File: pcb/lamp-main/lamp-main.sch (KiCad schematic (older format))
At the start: 37 parts, among them IC1 ATMEGA328P, IC2 LM1117, IC3 TLC5973, J1 5V_OUT, J2 LED_CARD_BOTTOM, P1 7-12V_IN, P2 AVR_ISP, P3 SERIAL, P4 LEDSTACK, P5 LEDSTACK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

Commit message: this is going somewhere
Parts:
- removed C10, C11: 0.1uF, symbol C
- removed IC3: TLC5973, symbol TLC5973
- removed J2: LED_CARD_BOTTOM, symbol 5PIN_FEMALE
- removed LED1, LED2: CREE-CLV6A-FKB, symbol CREE-CLV6A-FKB
- removed P7: LED_CARD_TOP, symbol 5PIN_MALE
- removed P8: SER_SHORT, symbol 5PIN_MALE
- removed R4: 2kΩ, symbol R
- removed R5: 1kΩ, symbol R
- removed S1: TOP, symbol SPDT
- LED_HRT: renamed from LED3; value HEART -> RED
- LED_PWR: renamed from LED4; value PWR -> RED
- P1: value 7-12V_IN -> 5-12V_IN
- Y1: value 14.7456MHz -> 8MHz
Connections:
- net labels added: ADC_6, ADC_7, ADC_C3, ADC_C4, ADC_C5, DIO_B1, DIO_B2, DIO_D4, INT_0, INT_1
- net labels removed: BLU, GRN, LED_GND, LED_SER_IN, LED_SER_OUT, RED, SENSE_BOT, SENSE_TOP, VLED, VLOG, VLOG_TOP
- wire segments 143 -> 101
- no-connect marks 10 -> 2
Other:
- note added: "3.3V input and optional regulator"
- note removed: "7-12 V Input/Output and 5V Regulator"
- note removed: "LED Board (Multiple)"
- moved on the sheet: LED_HRT, LED_PWR, R1, R2, R3, R6, R7

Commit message: main board edits first pass done
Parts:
- removed J1: 5V_OUT, symbol 2PIN_FEMALE
- added P10: VCC, symbol 2PIN_MALE
- added P7: USER-INPUT, symbol 5PIN_MALE
- added P8: EXTRA-IO, symbol 2PIN_MALE
- added P9: WIFI, symbol 3PIN_MALE
- C7: value 10uF -> DNP(10uF)
- C8: value 22uF -> DNP(22uF)
- IC2: value LM1117 -> DNP(LM1117_3.3)
- P1: value 5-12V_IN -> VLED_IN
- Y1: Distrib. Link http://www.digikey.com/product-detail/en/ABLS-14.7456MHZ-B4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 -> http://www.digikey.com/product-detail/en/ABM2-8.000MHZ-D4Y-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; Distrib. Part 535-10223-1-ND -> 535-10870-1-ND; Manuf. Part ABLS-14.7456MHZ-B4-T -> ABM2-8.000MHZ-D4Y-T
- renumbered LED_HRT to LED1, LED_PWR to LED2
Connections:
- net labels added: BUTTON_0, BUTTON_1, POT_0, POT_1, POT_2, WIFI_EN, WIFI_IRQ, WIFI_SS
- net labels removed: ADC_6, ADC_7, ADC_C5, DIO_B1, DIO_B2, DIO_D4, INT_0, INT_1
- wire segments 101 -> 113
- no-connect marks 2 -> 0
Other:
- note added: "ATMega 328P microcontroller"
- note added: "led stacks"
- note added: "programming and communication"
- note added: "user input and extra io"
- note removed: "LED Stack Headers"
- note removed: "MCU"
- note removed: "Programming and Communication Headers"
- moved on the sheet: C9, LED1, LED2, P2, P3, R6, R7

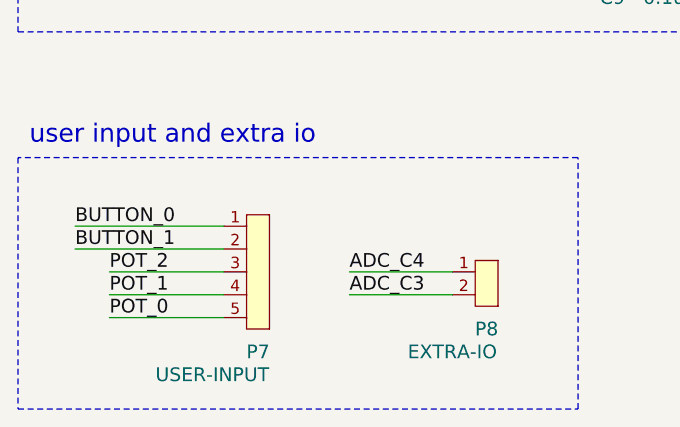
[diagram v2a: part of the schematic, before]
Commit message: still need to add boost reg to schematic;
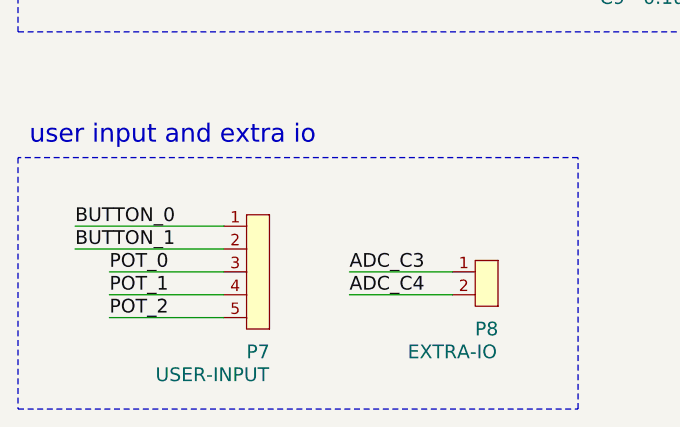
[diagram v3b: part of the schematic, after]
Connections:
- net ADC_C3: now also P8.1; no longer P8.2
- net ADC_C4: now also P8.2; no longer P8.1
- net POT_0: now also P7.3; no longer P7.5
- net POT_2: now also P7.5; no longer P7.3
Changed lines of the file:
@@
 Text Label 1100 6550 0    60   ~ 0
 BUTTON_1
-Text Label 1250 6650 0    60   ~ 0
+Text Label 1250 6850 0    60   ~ 0
 POT_2
 Text Label 1250 6750 0    60   ~ 0
 POT_1
-Text Label 1250 6850 0    60   ~ 0
+Text Label 1250 6650 0    60   ~ 0
 POT_0
 Wire Wire Line
@@
 	1    0    0    -1
 $EndComp
+Text Label 2300 6750 0    60   ~ 0
+ADC_C4
 Text Label 2300 6650 0    60   ~ 0
-ADC_C4
-Text Label 2300 6750 0    60   ~ 0
 ADC_C3
 Wire Wire Line

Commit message: trying something new
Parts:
- added JP?: VLED-VIN-JUMP, symbol JUMPER_2-PIN
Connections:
- net VCC: no longer P10.1
- net VIN: now also P10.1, JP?.2; no longer P1.1, P4.1, P5.1, P6.1
- new net VL: JP?.1, P1.1, P4.1, P5.1, P6.1
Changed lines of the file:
@@
 $EndComp
 Text Label 6850 3850 0    60   ~ 0
-VIN
+VL
 $Comp
 L GND #PWR09
@@
 $EndComp
 Text Label 7100 1100 0    60   ~ 0
-VIN
+VL
 $Comp
 L VCC #PWR016
@@
 	1    0    0    -1
 $EndComp
-Text Label 7100 1800 0    60   ~ 0
-VIN
 $Comp
 L VCC #PWR018
@@
 	1    0    0    -1
 $EndComp
-Text Label 7100 2500 0    60   ~ 0
-VIN
 $Comp
 L VCC #PWR020
@@
 	6500 3500 10000 3500
 Wire Notes Line
-	6500 4800 10000 4800
-Wire Notes Line
 	6500 3500 6500 4800
 Wire Wire Line
@@
 	9400 4050 9600 4050
 Wire Notes Line
-	10000 4800 10000 3500
+	10000 3500 10000 4800
 $Comp
 L C C3
@@
 	1    0    0    -1
 $EndComp
-$Comp
-L VCC #PWR026
-U 1 1 5310DE0A
-P 6950 4350
-F 0 "#PWR026" H 6950 4450 30  0001 C CNN
-F 1 "VCC" H 6950 4450 30  0000 C CNN
-F 2 "" H 6950 4350 60  0000 C CNN
-F 3 "" H 6950 4350 60  0000 C CNN
-	1    6950 4350
-	0    -1   1    0
-$EndComp
-Wire Wire Line
-	6950 4350 7050 4350
+Wire Wire Line
+	6850 4350 7050 4350
 $Comp
 L R R6
@@
 Wire Wire Line
 	2250 3250 2350 3250
+Text Label 7100 1800 0    60   ~ 0
+VL
+Text Label 7100 2500 0    60   ~ 0
+VL
+Text Label 6850 4350 0    60   ~ 0
+VIN
+$Comp
+L JUMPER_2-PIN JP?
+U 1 1 5363ED03
+P 7100 4900
+F 0 "JP?" H 7100 5000 60  0000 C CNN
+F 1 "VLED-VIN-JUMP" H 7100 4800 60  0000 C CNN
+F 2 "" H 7000 4900 60  0001 C CNN
+F 3 "" H 7100 5000 60  0001 C CNN
+	1    7100 4900
+	1    0    0    -1
+$EndComp
+Text Label 6750 4900 0    60   ~ 0
+VL
+Text Label 7450 4900 2    60   ~ 0
+VIN
+Wire Wire Line
+	7450 4900 7250 4900
+Wire Wire Line
+	6750 4900 6950 4900
 $EndSCHEMATC

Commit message: board layout and schematic refinement
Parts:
- removed P9: WIFI, symbol 3PIN_MALE
- P10: value VCC -> V_IN
- P8: value EXTRA-IO -> EXTRA-ADC
- gave numbers to parts that had none: 1
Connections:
- net WIFI_IRQ is gone; now on net BUTTON_0: IC1.32 (PD2(INT0/PCINT18))
- net BUTTON_0: no longer IC1.1 (PD3(PCINT19/OC2B/INT1))
- net BUTTON_1: now also IC1.1 (PD3(PCINT19/OC2B/INT1)); no longer IC1.2 (PD4(PCINT20/XCK/T0))
- net POT_0: now also IC1.26 (PC3(ADC3/PCINT11)); no longer IC1.28 (PC5(ADC5/SCL/PCINT13))
- net POT_1: now also IC1.27 (PC4(ADC4/SDA/PCINT12)); no longer IC1.19 (ADC6)
- net POT_2: now also IC1.28 (PC5(ADC5/SCL/PCINT13)); no longer IC1.22 (ADC7)
- net ADC_C3 renamed ADC7
- net ADC7: now also IC1.22 (ADC7); no longer IC1.26 (PC3(ADC3/PCINT11))
- net ADC_C4 renamed ADC6
- net ADC6: now also IC1.19 (ADC6); no longer IC1.27 (PC4(ADC4/SDA/PCINT12))
- net WIFI_EN: no longer names the net of IC1.13 (PB1(PCINT1/OC1A))
- net WIFI_SS: no longer names the net of IC1.14 (PB2(PCINT2/~SS~/OC1B))
- no-connect marks 0 -> 3
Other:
- note added: "user input and wifi io"
- note removed: "user input and extra io"
- moved on the sheet: P7, P8

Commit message: still working on the layout
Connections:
- net BUTTON_1 renamed WIFI_IRQ
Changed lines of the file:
@@
 Text Label 4750 3250 2    60   ~ 0
 ADC6
-Text Label 4850 2500 2    60   ~ 0
-WIFI_IRQ
 Text Label 5600 2500 2    60   ~ 0
 BUTTON_0
-Text Label 5600 2400 2    60   ~ 0
-BUTTON_1
 $Comp
 L C C9
@@
 Text Label 1000 6850 0    60   ~ 0
 WIFI_SS
-Text Label 1000 6450 0    60   ~ 0
+Text Label 1500 6550 0    60   ~ 0
 WIFI_IRQ
 Text Label 4750 1250 2    60   ~ 0
@@
 Text Label 1500 6450 0    60   ~ 0
 BUTTON_0
-Text Label 1500 6550 0    60   ~ 0
-BUTTON_1
 Text Label 1650 6850 0    60   ~ 0
 POT_2
@@
 	2150 6550 1500 6550
 Wire Wire Line
-	1000 6450 2150 6450
-Wire Wire Line
 	3350 6700 2900 6700
 Wire Wire Line
@@
 NoConn ~ 2350 3050
 NoConn ~ 2350 3150
+Text Label 5600 2400 2    60   ~ 0
+WIFI_IRQ
+Wire Wire Line
+	1500 6450 2150 6450
 $EndSCHEMATC

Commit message: several boards
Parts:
- C1, C2, C3, C4, C5, C6, C9: footprint (none) -> capacitor:0603(1608m)-CHIP-CAP
- C7, C8: footprint (none) -> capacitor:1206(3216m)-CHIP-CAP
- IC1: footprint (none) -> qfp:TQFP32_P0.8mm
- IC2: footprint (none) -> sot:SOT223
- JP1: footprint (none) -> jumper:SOLDER-JUMPER_1-WAY
- LED1, LED2: footprint (none) -> led:0603(1608m)-SM-LED
- P1, P10, P8: footprint (none) -> sip:SIP2
- P2: footprint (none) -> connect-thru:2x3-ARRAY_P100mil
- P3: footprint (none) -> sip:SIP6
- P4, P5, P6, P7: footprint (none) -> sip:SIP5
- R1, R2, R3, R6, R7: footprint (none) -> resistor:0603(1608m)-CHIP-RESISTOR
- Y1: footprint (none) -> crystal:ABRACON-ABM2_xtal
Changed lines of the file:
@@
 F 0 "IC1" H 2650 3400 60  0000 C CNN
 F 1 "ATMEGA328P" H 3700 1050 60  0000 C CNN
-F 2 "" H 3350 2250 60  0000 C CNN
+F 2 "qfp:TQFP32_P0.8mm" H 3350 2250 60  0000 C CNN
 F 3 "" H 3350 2250 60  0000 C CNN
 F 4 "Atmel" H 3350 2250 60  0001 C CNN "Manufacturer"
@@
 F 0 "P2" H 1700 5300 60  0000 C CNN
 F 1 "AVR_ISP" H 2100 5300 60  0000 C CNN
-F 2 "" H 1950 5100 60  0001 C CNN
+F 2 "connect-thru:2x3-ARRAY_P100mil" H 1950 5100 60  0001 C CNN
 F 3 "" H 1950 5100 60  0001 C CNN
 	1    1950 5100
@@
 F 0 "P3" H 4050 5550 60  0000 C CNN
 F 1 "SERIAL" H 4000 5450 60  0000 C CNN
-F 2 "" H 4100 5050 60  0001 C CNN
+F 2 "sip:SIP6" H 4100 5050 60  0001 C CNN
 F 3 "" H 4100 5050 60  0001 C CNN
 	1    4050 5050
@@
 F 0 "Y1" V 2200 2700 60  0000 C CNN
 F 1 "8MHz" V 2100 2700 60  0000 C CNN
-F 2 "" H 2150 2500 60  0001 C CNN
+F 2 "crystal:ABRACON-ABM2_xtal" H 2150 2500 60  0001 C CNN
 F 3 "http://www.abracon.com/Resonators/abm2.pdf" H 2150 2500 60  0001 C CNN
 F 4 "Abracon Corporation" H 2150 2500 60  0001 C CNN "Manufacturer"
@@
 F 0 "C2" H 1350 2550 60  0000 C CNN
 F 1 "24pF" H 1600 2550 60  0000 C CNN
-F 2 "" H 1500 2400 60  0001 C CNN
+F 2 "capacitor:0603(1608m)-CHIP-CAP" H 1500 2400 60  0001 C CNN
 F 3 "" H 1500 2400 60  0001 C CNN
 F 4 "Samsung" H 1500 2400 60  0001 C CNN "Manufacturer"
@@
 F 0 "C6" H 1950 2450 60  0000 C CNN
 F 1 "0.1uF" H 1950 2350 60  0000 C CNN
-F 2 "" H 2100 2250 60  0001 C CNN
+F 2 "capacitor:0603(1608m)-CHIP-CAP" H 2100 2250 60  0001 C CNN
 F 3 "" H 2100 2250 60  0001 C CNN
 F 4 "On hand" H 2100 2250 60  0001 C CNN "Distributor"
@@
 F 0 "C1" V 1650 1750 60  0000 C CNN
 F 1 "0.1uF" V 1550 1750 60  0000 C CNN
-F 2 "" H 1350 1750 60  0001 C CNN
+F 2 "capacitor:0603(1608m)-CHIP-CAP" H 1350 1750 60  0001 C CNN
 F 3 "" H 1350 1750 60  0001 C CNN
 F 4 "On Hand" H 1350 1750 60  0001 C CNN "Distributor"
@@
 F 0 "C4" V 1950 1750 60  0000 C CNN
 F 1 "0.1uF" V 1850 1750 60  0000 C CNN
-F 2 "" H 1650 1750 60  0001 C CNN
+F 2 "capacitor:0603(1608m)-CHIP-CAP" H 1650 1750 60  0001 C CNN
 F 3 "" H 1650 1750 60  0001 C CNN
 F 4 "On hand" H 1650 1750 60  0001 C CNN "Distributor"
@@
 F 0 "C5" V 2250 1750 60  0000 C CNN
 F 1 "0.1uF" V 2150 1750 60  0000 C CNN
-F 2 "" H 1950 1750 60  0001 C CNN
+F 2 "capacitor:0603(1608m)-CHIP-CAP" H 1950 1750 60  0001 C CNN
 F 3 "" H 1950 1750 60  0001 C CNN
 F 4 "On hand" H 1950 1750 60  0001 C CNN "Distributor"
@@
 F 0 "P1" H 7350 3900 60  0000 C CNN
 F 1 "VLED_IN" H 7050 3700 60  0000 C CNN
-F 2 "" H 7100 3700 60  0001 C CNN
+F 2 "sip:SIP2" H 7100 3700 60  0001 C CNN
 F 3 "" H 7100 3700 60  0001 C CNN
 	1    7150 3900
@@
 F 0 "IC2" H 8400 4500 60  0000 C CNN
 F 1 "DNP(LM1117_3.3)" H 8400 4400 60  0000 C CNN
-F 2 "" H 8400 4100 60  0001 C CNN
+F 2 "sot:SOT223" H 8400 4100 60  0001 C CNN
 F 3 "http://www.diodes.com/datasheets/AZ1117C.pdf" H 8400 4100 60  0001 C CNN
 F 4 "Diodes Incorporated" H 8400 4100 60  0001 C CNN "Manufacturer"
@@
 F 0 "C7" V 7850 4550 60  0000 C CNN
 F 1 "DNP(10uF)" V 7950 4700 60  0000 C CNN
-F 2 "" H 7850 4400 60  0001 C CNN
+F 2 "capacitor:1206(3216m)-CHIP-CAP" H 7850 4400 60  0001 C CNN
 F 3 "" H 7850 4400 60  0001 C CNN
 F 4 "Taiyo Yuden" H 7850 4400 60  0001 C CNN "Manufacturer"
@@
 F 0 "C8" V 8900 4500 60  0000 C CNN
 F 1 "DNP(22uF)" V 9000 4650 60  0000 C CNN
-F 2 "" H 8900 4300 60  0001 C CNN
+F 2 "capacitor:1206(3216m)-CHIP-CAP" H 8900 4300 60  0001 C CNN
 F 3 "" H 8900 4300 60  0001 C CNN
 F 4 "Taiyo Yuden" H 8900 4300 60  0001 C CNN "Manufacturer"
@@
 F 0 "R2" H 5400 1400 60  0000 C CNN
 F 1 "10kΩ" H 5700 1400 60  0000 C CNN
-F 2 "" H 5350 1700 60  0001 C CNN
+F 2 "resistor:0603(1608m)-CHIP-RESISTOR" H 5350 1700 60  0001 C CNN
 F 3 "" H 5350 1700 60  0001 C CNN
 F 4 "On hand" H 5350 1700 60  0001 C CNN "Distributor"
@@
 F 0 "R3" H 5400 1500 60  0000 C CNN
 F 1 "10kΩ" H 5700 1500 60  0000 C CNN
-F 2 "" H 5350 1800 60  0001 C CNN
+F 2 "resistor:0603(1608m)-CHIP-RESISTOR" H 5350 1800 60  0001 C CNN
 F 3 "" H 5350 1800 60  0001 C CNN
 F 4 "On hand" H 5350 1800 60  0001 C CNN "Distributor"
@@
 F 0 "P4" H 7650 1500 60  0000 C CNN
 F 1 "LEDSTACK" H 7800 1400 60  0000 C CNN
-F 2 "" H 7500 1200 60  0001 C CNN
+F 2 "sip:SIP5" H 7500 1200 60  0001 C CNN
 F 3 "" H 7500 1200 60  0001 C CNN
 	1    7450 1300
@@
 F 0 "P5" H 7650 2200 60  0000 C CNN
 F 1 "LEDSTACK" H 7800 2100 60  0000 C CNN
-F 2 "" H 7500 1900 60  0001 C CNN
+F 2 "sip:SIP5" H 7500 1900 60  0001 C CNN
 F 3 "" H 7500 1900 60  0001 C CNN
 	1    7450 2000
@@
 F 0 "P6" H 7650 2900 60  0000 C CNN
 F 1 "LEDSTACK" H 7800 2800 60  0000 C CNN
-F 2 "" H 7500 2600 60  0001 C CNN
+F 2 "sip:SIP5" H 7500 2600 60  0001 C CNN
 F 3 "" H 7500 2600 60  0001 C CNN
 	1    7450 2700
@@
 F 0 "C3" H 1350 2450 60  0000 C CNN
 F 1 "24pF" H 1600 2450 60  0000 C CNN
-F 2 "" H 1500 2600 60  0001 C CNN
+F 2 "capacitor:0603(1608m)-CHIP-CAP" H 1500 2600 60  0001 C CNN
 F 3 "" H 1500 2600 60  0001 C CNN
 F 4 "Samsung Electro-Mechanics America, Inc" H 1500 2600 60  0001 C CNN "Manufacturer"
@@
 F 0 "R6" H 1950 3250 60  0000 C CNN
 F 1 "1kΩ" H 2150 3250 60  0000 C CNN
-F 2 "" H 2000 3350 60  0001 C CNN
+F 2 "resistor:0603(1608m)-CHIP-RESISTOR" H 2000 3350 60  0001 C CNN
 F 3 "" H 2000 3350 60  0001 C CNN
 F 4 "On hand" H 2000 3350 60  0001 C CNN "Distributor"
@@
 F 0 "LED1" H 1450 3450 60  0000 C CNN
 F 1 "RED" H 1750 3450 60  0000 C CNN
-F 2 "" H 1600 3350 60  0001 C CNN
+F 2 "led:0603(1608m)-SM-LED" H 1600 3350 60  0001 C CNN
 F 3 "" H 1600 3350 60  0001 C CNN
 F 4 "On hand" H 1600 3350 60  0001 C CNN "Distributor"
@@
 F 0 "R7" H 1950 3500 60  0000 C CNN
 F 1 "1kΩ" H 2150 3500 60  0000 C CNN
-F 2 "" H 2000 3600 60  0001 C CNN
+F 2 "resistor:0603(1608m)-CHIP-RESISTOR" H 2000 3600 60  0001 C CNN
 F 3 "" H 2000 3600 60  0001 C CNN
 F 4 "On hand" H 2000 3600 60  0001 C CNN "Distributor"
@@
 F 0 "LED2" H 1450 3700 60  0000 C CNN
 F 1 "RED" H 1750 3700 60  0000 C CNN
-F 2 "" H 1600 3600 60  0001 C CNN
+F 2 "led:0603(1608m)-SM-LED" H 1600 3600 60  0001 C CNN
 F 3 "" H 1600 3600 60  0001 C CNN
 F 4 "On hand" H 1600 3600 60  0001 C CNN "Distributor"
@@
 F 0 "R1" H 5400 1300 60  0000 C CNN
 F 1 "10kΩ" H 5700 1300 60  0000 C CNN
-F 2 "" H 5350 1600 60  0001 C CNN
+F 2 "resistor:0603(1608m)-CHIP-RESISTOR" H 5350 1600 60  0001 C CNN
 F 3 "" H 5350 1600 60  0001 C CNN
 F 4 "On hand" H 5350 1600 60  0001 C CNN "Distributor"
@@
 F 0 "C9" H 3450 5150 60  0000 C CNN
 F 1 "0.1uF" H 3700 5150 60  0000 C CNN
-F 2 "" H 3750 5300 60  0001 C CNN
+F 2 "capacitor:0603(1608m)-CHIP-CAP" H 3750 5300 60  0001 C CNN
 F 3 "" H 3750 5300 60  0001 C CNN
 F 4 "On hand" H 3750 5300 60  0001 C CNN "Distributor"
@@
 F 0 "P7" H 2300 6300 60  0000 C CNN
 F 1 "USER-INPUT" H 2100 6200 60  0000 C CNN
-F 2 "" H 2300 6550 60  0001 C CNN
+F 2 "sip:SIP5" H 2300 6550 60  0001 C CNN
 F 3 "" H 2300 6550 60  0001 C CNN
 	1    2250 6650
@@
 F 0 "P8" H 3500 6450 60  0000 C CNN
 F 1 "EXTRA-ADC" H 3350 6350 60  0000 C CNN
-F 2 "" H 3400 6450 60  0001 C CNN
+F 2 "sip:SIP2" H 3400 6450 60  0001 C CNN
 F 3 "" H 3400 6450 60  0001 C CNN
 	1    3450 6650
@@
 F 0 "P10" H 7350 4400 60  0000 C CNN
 F 1 "V_IN" H 7150 4200 60  0000 C CNN
-F 2 "" H 7100 4200 60  0001 C CNN
+F 2 "sip:SIP2" H 7100 4200 60  0001 C CNN
 F 3 "" H 7100 4200 60  0001 C CNN
 	1    7150 4400
@@
 F 0 "JP1" H 7100 5000 60  0000 C CNN
 F 1 "VLED-VIN-JUMP" H 7100 4800 60  0000 C CNN
-F 2 "" H 7000 4900 60  0001 C CNN
+F 2 "jumper:SOLDER-JUMPER_1-WAY" H 7000 4900 60  0001 C CNN
 F 3 "" H 7100 5000 60  0001 C CNN
 	1    7100 4900
